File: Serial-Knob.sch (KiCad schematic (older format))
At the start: 17 parts, among them IC1 ATTINY85-S, P1 CONN_4

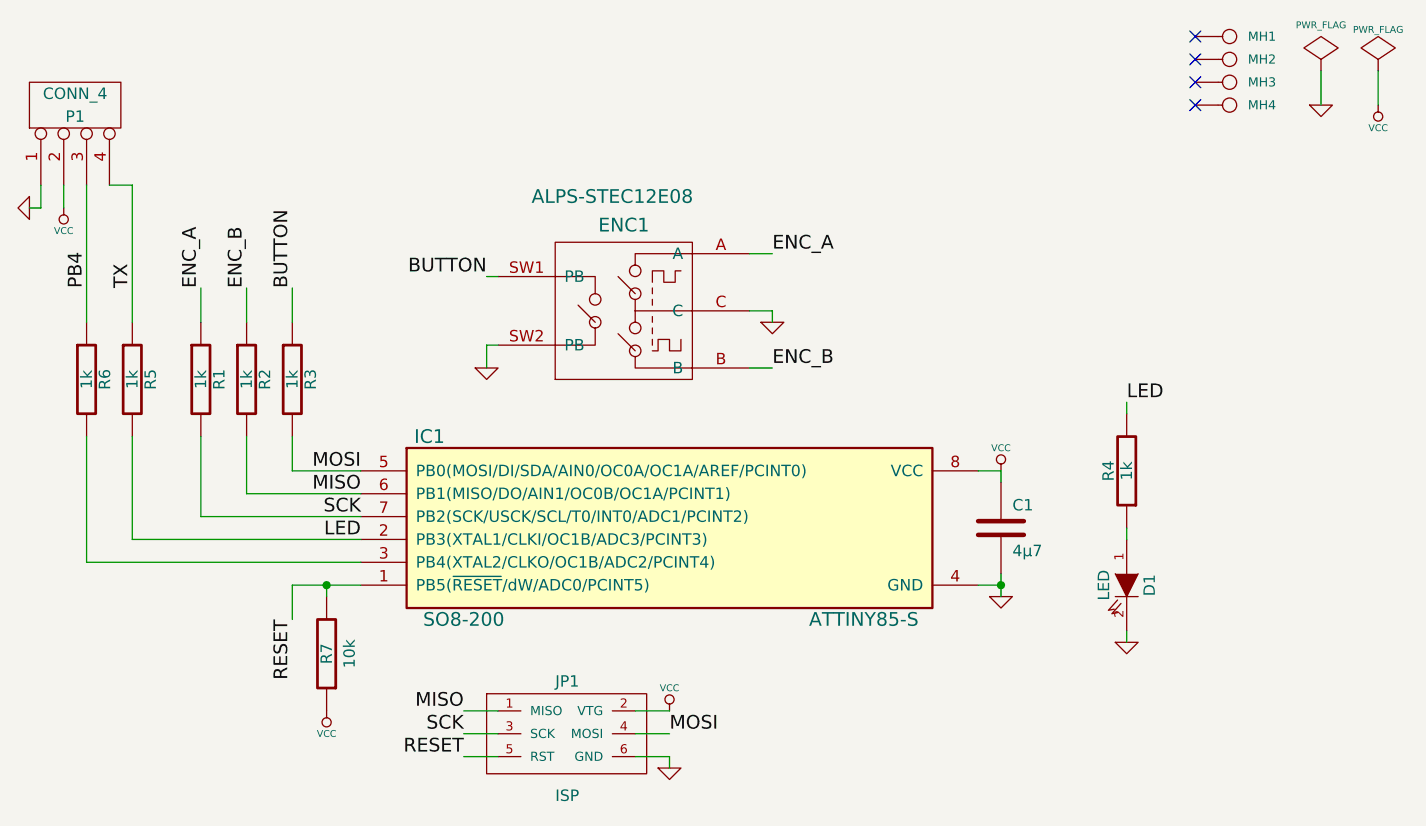
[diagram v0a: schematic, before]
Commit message: Changed all vias to 0.65/0.35 + moved to 1206 resistor packs (4x).
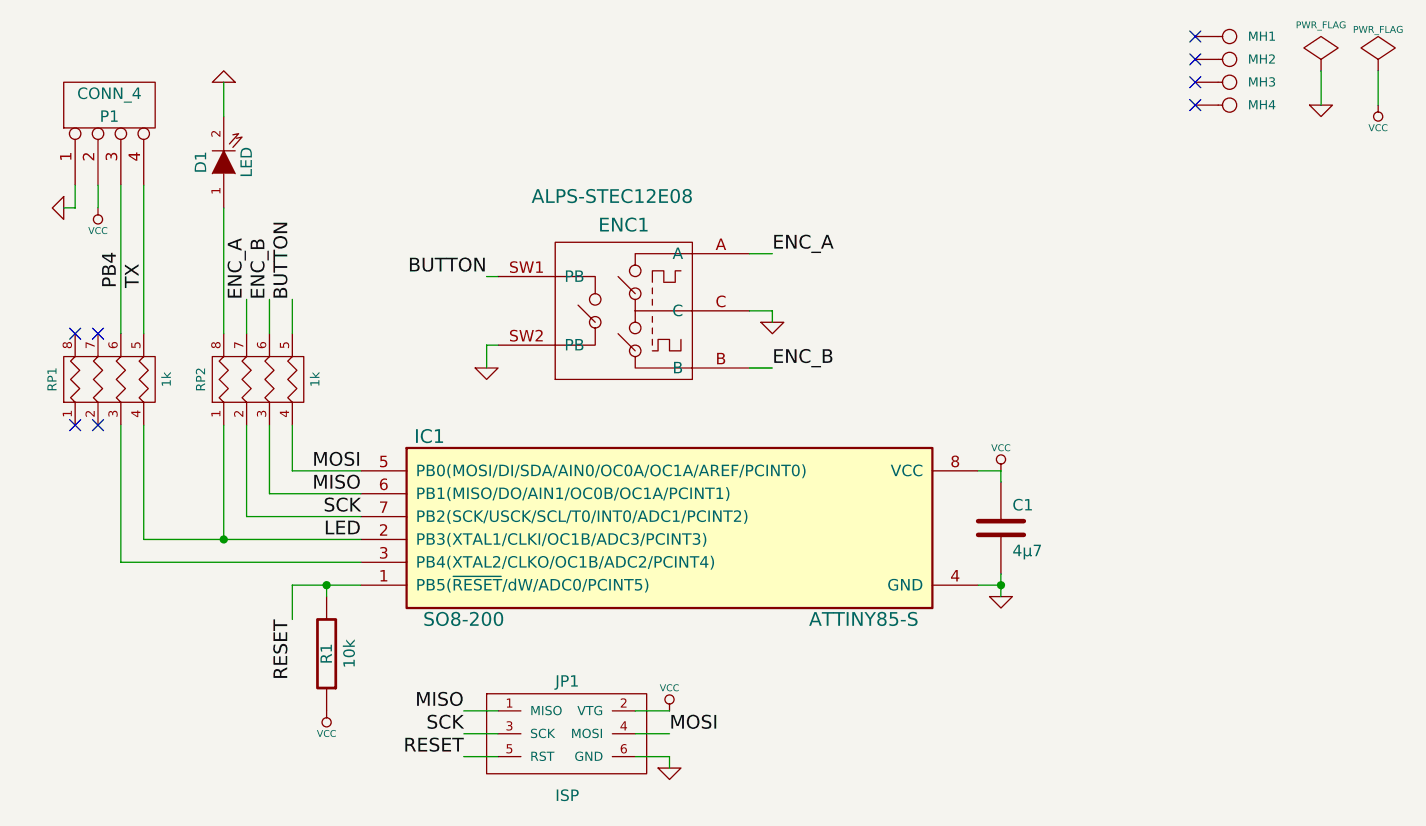
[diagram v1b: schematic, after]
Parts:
- removed R1, R2, R3, R4, R5, R6: 1k, symbol R
- added RP1, RP2: 1k, symbol R_PACK4
- renumbered R7 to R1
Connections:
- net BUTTON: now also RP2.5 (R4)
- net ENC_A: now also RP2.7 (R2)
- net ENC_B: now also RP2.6 (R3)
- net LED: now also RP1.4 (P4), RP2.1 (P1)
- net MISO: now also RP2.3 (P3)
- net MOSI: now also RP2.4 (P4)
- net PB4: now also RP1.6 (R3)
- net SCK: now also RP2.2 (P2)
- net TX: now also RP1.5 (R4)
- net at D1.1 (A): now also RP2.8 (R1)
- net at IC1.3 (PB4(XTAL2/CLKO/OC1B/ADC2/PCINT4)): now also RP1.3 (P3)
- no-connect marks 4 -> 8
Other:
- moved on the sheet: D1, P1
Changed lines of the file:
@@
-EESchema Schematic File Version 2  date Wed 27 Feb 2013 09:12:17 AM CET
+EESchema Schematic File Version 2  date Fri 01 Mar 2013 09:15:15 AM CET
 LIBS:my_parts
 LIBS:power
@@
 Sheet 1 1
 Title "Serial Knob - a.k.a. \"The Knob\""
-Date "23 feb 2013"
-Rev "0.1"
+Date "1 mar 2013"
+Rev "0.2"
 Comp "2013 - blog.spitzenpfeil.org"
 Comment1 ""
@@
 	1    0    0    -1
 $EndComp
-Text Label 2200 1950 1    60   ~ 0
+Text Label 2400 2000 1    60   ~ 0
 ENC_A
-Text Label 2400 1950 1    60   ~ 0
+Text Label 2500 2000 1    60   ~ 0
 ENC_B
-Text Label 2600 1950 1    60   ~ 0
+Text Label 2600 2000 1    60   ~ 0
 BUTTON
 $Comp
@@
 $EndComp
 $Comp
-L R R7
+L R R1
 U 1 1 4F6EC6DD
 P 2750 3550
-F 0 "R7" V 2750 3550 50  0000 C CNN
+F 0 "R1" V 2750 3550 50  0000 C CNN
 F 1 "10k" V 2650 3550 50  0000 C CNN
 F 2 "" H 2750 3550 60  0001 C CNN
@@
 $EndComp
 Connection ~ 2750 3250
-Wire Wire Line
-	2400 2850 2900 2850
-Wire Wire Line
-	2200 2950 2900 2950
 Wire Wire Line
 	2600 3250 2900 3250
@@
 L LED D1
 U 1 1 50EDA6CA
-P 6250 3250
-F 0 "D1" H 6250 3350 50  0000 C CNN
-F 1 "LED" H 6250 3150 50  0000 C CNN
-F 2 "" H 6250 3250 60  0001 C CNN
-F 3 "" H 6250 3250 60  0001 C CNN
-	1    6250 3250
-	0    1    1    0
+P 2300 1400
+F 0 "D1" H 2300 1500 50  0000 C CNN
+F 1 "LED" H 2300 1300 50  0000 C CNN
+F 2 "" H 2300 1400 60  0001 C CNN
+F 3 "" H 2300 1400 60  0001 C CNN
+	1    2300 1400
+	0    -1   -1   0
 $EndComp
 $Comp
 L GND #PWR06
-U 1 1 50EDA6D9
-P 6250 3500
-F 0 "#PWR06" H 6250 3500 30  0001 C CNN
-F 1 "GND" H 6250 3430 30  0001 C CNN
-F 2 "" H 6250 3500 60  0001 C CNN
-F 3 "" H 6250 3500 60  0001 C CNN
-	1    6250 3500
-	1    0    0    -1
-$EndComp
-$Comp
-L R R4
-U 1 1 50EDA6E8
-P 6250 2750
-F 0 "R4" V 6330 2750 50  0000 C CNN
-F 1 "1k" V 6250 2750 50  0000 C CNN
-F 2 "" H 6250 2750 60  0001 C CNN
-F 3 "" H 6250 2750 60  0001 C CNN
-	1    6250 2750
-	-1   0    0    1
-$EndComp
-Wire Wire Line
-	6250 3450 6250 3500
-Wire Wire Line
-	6250 3050 6250 3000
-Wire Wire Line
-	6250 2450 6250 2500
-$Comp
-L GND #PWR07
 U 1 1 50FE45EC
 P 3450 2300
-F 0 "#PWR07" H 3450 2300 30  0001 C CNN
+F 0 "#PWR06" H 3450 2300 30  0001 C CNN
 F 1 "GND" H 3450 2230 30  0001 C CNN
 F 2 "" H 3450 2300 60  0001 C CNN
@@
 	4700 2050 4700 2100
 $Comp
-L GND #PWR08
+L GND #PWR07
 U 1 1 50FE464A
 P 4700 2100
-F 0 "#PWR08" H 4700 2100 30  0001 C CNN
+F 0 "#PWR07" H 4700 2100 30  0001 C CNN
 F 1 "GND" H 4700 2030 30  0001 C CNN
 F 2 "" H 4700 2100 60  0001 C CNN
@@
 Text Label 3450 1900 2    60   ~ 0
 BUTTON
-$Comp
-L R R1
-U 1 1 50FE472E
-P 2200 2350
-F 0 "R1" V 2280 2350 50  0000 C CNN
-F 1 "1k" V 2200 2350 50  0000 C CNN
-F 2 "" H 2200 2350 60  0001 C CNN
-F 3 "" H 2200 2350 60  0001 C CNN
-	1    2200 2350
-	1    0    0    -1
-$EndComp
-$Comp
-L R R2
-U 1 1 50FE473D
-P 2400 2350
-F 0 "R2" V 2480 2350 50  0000 C CNN
-F 1 "1k" V 2400 2350 50  0000 C CNN
-F 2 "" H 2400 2350 60  0001 C CNN
-F 3 "" H 2400 2350 60  0001 C CNN
-	1    2400 2350
-	1    0    0    -1
-$EndComp
-$Comp
-L R R3
-U 1 1 50FE474C
-P 2600 2350
-F 0 "R3" V 2680 2350 50  0000 C CNN
-F 1 "1k" V 2600 2350 50  0000 C CNN
-F 2 "" H 2600 2350 60  0001 C CNN
-F 3 "" H 2600 2350 60  0001 C CNN
-	1    2600 2350
-	1    0    0    -1
-$EndComp
-Wire Wire Line
-	2600 2600 2600 2750
-Wire Wire Line
-	2400 2600 2400 2850
-Wire Wire Line
-	2200 2600 2200 2950
-Wire Wire Line
-	2600 1950 2600 2100
-Wire Wire Line
-	2400 1950 2400 2100
-Wire Wire Line
-	2200 1950 2200 2100
 Wire Wire Line
 	2600 2750 2900 2750
-Text Label 1900 1950 1    60   ~ 0
+Text Label 1950 1950 1    60   ~ 0
 TX
 Wire Wire Line
@@
 Text Label 2900 3050 2    60   ~ 0
 LED
-Text Label 6250 2450 0    60   ~ 0
-LED
 $Comp
 L CONN_4 P1
 U 1 1 50FE4A96
-P 1650 1150
-F 0 "P1" V 1600 1150 50  0000 C CNN
-F 1 "CONN_4" V 1700 1150 50  0000 C CNN
-F 2 "" H 1650 1150 60  0001 C CNN
-F 3 "" H 1650 1150 60  0001 C CNN
-	1    1650 1150
+P 1800 1150
+F 0 "P1" V 1750 1150 50  0000 C CNN
+F 1 "CONN_4" V 1850 1150 50  0000 C CNN
+F 2 "" H 1800 1150 60  0001 C CNN
+F 3 "" H 1800 1150 60  0001 C CNN
+	1    1800 1150
 	0    -1   -1   0
 $EndComp
 Wire Wire Line
-	1600 1500 1600 1600
-Wire Wire Line
-	1500 1500 1500 1600
-$Comp
-L GND #PWR09
+	1750 1500 1750 1600
+Wire Wire Line
+	1650 1500 1650 1600
+$Comp
+L GND #PWR08
 U 1 1 50FE4B02
-P 1450 1600
-F 0 "#PWR09" H 1450 1600 30  0001 C CNN
-F 1 "GND" H 1450 1530 30  0001 C CNN
-F 2 "" H 1450 1600 60  0001 C CNN
-F 3 "" H 1450 1600 60  0001 C CNN
-	1    1450 1600
-	0    1    1    0
-$EndComp
-Wire Wire Line
-	1500 1600 1450 1600
-$Comp
-L VCC #PWR010
-U 1 1 50FE4B43
 P 1600 1600
-F 0 "#PWR010" H 1600 1700 30  0001 C CNN
-F 1 "VCC" H 1600 1700 30  0000 C CNN
+F 0 "#PWR08" H 1600 1600 30  0001 C CNN
+F 1 "GND" H 1600 1530 30  0001 C CNN
 F 2 "" H 1600 1600 60  0001 C CNN
 F 3 "" H 1600 1600 60  0001 C CNN
 	1    1600 1600
+	0    1    1    0
+$EndComp
+Wire Wire Line
+	1650 1600 1600 1600
+$Comp
+L VCC #PWR09
+U 1 1 50FE4B43
+P 1750 1600
+F 0 "#PWR09" H 1750 1700 30  0001 C CNN
+F 1 "VCC" H 1750 1700 30  0000 C CNN
+F 2 "" H 1750 1600 60  0001 C CNN
+F 3 "" H 1750 1600 60  0001 C CNN
+	1    1750 1600
 	-1   0    0    1
 $EndComp
@@
 NoConn ~ 6550 950
 NoConn ~ 6550 850
-$Comp
-L R R5
-U 1 1 50FE56B2
-P 1900 2350
-F 0 "R5" V 1980 2350 50  0000 C CNN
-F 1 "1k" V 1900 2350 50  0000 C CNN
-F 2 "" H 1900 2350 60  0001 C CNN
-F 3 "" H 1900 2350 60  0001 C CNN
-	1    1900 2350
-	1    0    0    -1
-$EndComp
-$Comp
-L R R6
-U 1 1 50FE56C1
-P 1700 2350
-F 0 "R6" V 1780 2350 50  0000 C CNN
-F 1 "1k" V 1700 2350 50  0000 C CNN
-F 2 "" H 1700 2350 60  0001 C CNN
-F 3 "" H 1700 2350 60  0001 C CNN
-	1    1700 2350
-	1    0    0    -1
-$EndComp
-Wire Wire Line
-	1700 1500 1700 2100
-Text Label 1700 1950 1    60   ~ 0
+Text Label 1850 1950 1    60   ~ 0
 PB4
 $Comp
-L PWR_FLAG #FLG011
+L PWR_FLAG #FLG010
 U 1 1 50FE5769
 P 7350 1000
-F 0 "#FLG011" H 7350 1095 30  0001 C CNN
+F 0 "#FLG010" H 7350 1095 30  0001 C CNN
 F 1 "PWR_FLAG" H 7350 1180 30  0000 C CNN
 F 2 "" H 7350 1000 60  0001 C CNN
@@
 $EndComp
 $Comp
-L VCC #PWR012
+L VCC #PWR011
 U 1 1 50FE5778
 P 7350 1150
-F 0 "#PWR012" H 7350 1250 30  0001 C CNN
+F 0 "#PWR011" H 7350 1250 30  0001 C CNN
 F 1 "VCC" H 7350 1250 30  0000 C CNN
 F 2 "" H 7350 1150 60  0001 C CNN
@@
 Wire Wire Line
 	7350 1000 7350 1150
-Wire Wire Line
-	1900 1500 1900 2100
-Wire Wire Line
-	1900 2600 1900 3050
-Wire Wire Line
-	1900 3050 2900 3050
-Wire Wire Line
-	1700 2600 1700 3150
-Wire Wire Line
-	1700 3150 2900 3150
-Wire Wire Line
-	1800 1500 1900 1500
 Text Label 4250 3900 0    60   ~ 0
 MOSI
@@
 $EndComp
 $Comp
-L VCC #PWR013
+L VCC #PWR012
 U 1 1 50FF0F17
 P 4250 3800
-F 0 "#PWR013" H 4250 3900 30  0001 C CNN
+F 0 "#PWR012" H 4250 3900 30  0001 C CNN
 F 1 "VCC" H 4250 3900 30  0000 C CNN
 F 2 "" H 4250 3800 60  0001 C CNN
@@
 $EndComp
 $Comp
-L GND #PWR014
+L GND #PWR013
 U 1 1 50FF0F26
 P 4250 4050
-F 0 "#PWR014" H 4250 4050 30  0001 C CNN
+F 0 "#PWR013" H 4250 4050 30  0001 C CNN
 F 1 "GND" H 4250 3980 30  0001 C CNN
 F 2 "" H 4250 4050 60  0001 C CNN
@@
 	1    0    0    -1
 $EndComp
+$Comp
+L R_PACK4 RP2
+U 1 1 51305629
+P 2650 2350
+F 0 "RP2" H 2650 2800 40  0000 C CNN
+F 1 "1k" H 2650 2300 40  0000 C CNN
+F 2 "" H 2650 2350 60  0000 C CNN
+F 3 "" H 2650 2350 60  0000 C CNN
+	1    2650 2350
+	0    -1   -1   0
+$EndComp
+$Comp
+L R_PACK4 RP1
+U 1 1 51305642
+P 2000 2350
+F 0 "RP1" H 2000 2800 40  0000 C CNN
+F 1 "1k" H 2000 2300 40  0000 C CNN
+F 2 "" H 2000 2350 60  0000 C CNN
+F 3 "" H 2000 2350 60  0000 C CNN
+	1    2000 2350
+	0    -1   -1   0
+$EndComp
+Wire Wire Line
+	2600 2550 2600 2750
+Wire Wire Line
+	2500 2550 2500 2850
+Wire Wire Line
+	2400 2550 2400 2950
+Wire Wire Line
+	2500 2850 2900 2850
+Wire Wire Line
+	2400 2950 2900 2950
+Wire Wire Line
+	2300 2550 2300 3050
+Wire Wire Line
+	1950 3050 2900 3050
+Wire Wire Line
+	1950 3050 1950 2550
+Connection ~ 2300 3050
+Wire Wire Line
+	2600 2000 2600 2150
+Wire Wire Line
+	2500 2000 2500 2150
+Wire Wire Line
+	2400 2000 2400 2150
+Wire Wire Line
+	2300 1600 2300 2150
+$Comp
+L GND #PWR014
+U 1 1 51305895
+P 2300 1050
+F 0 "#PWR014" H 2300 1050 30  0001 C CNN
+F 1 "GND" H 2300 980 30  0001 C CNN
+F 2 "" H 2300 1050 60  0000 C CNN
+F 3 "" H 2300 1050 60  0000 C CNN
+	1    2300 1050
+	-1   0    0    1
+$EndComp
+Wire Wire Line
+	2300 1050 2300 1200
+Wire Wire Line
+	1950 1500 1950 2150
+Wire Wire Line
+	1850 1500 1850 2150
+Wire Wire Line
+	1850 2550 1850 3150
+Wire Wire Line
+	1850 3150 2900 3150
+NoConn ~ 1650 2550
+NoConn ~ 1750 2550
+NoConn ~ 1750 2150
+NoConn ~ 1650 2150
 $EndSCHEMATC

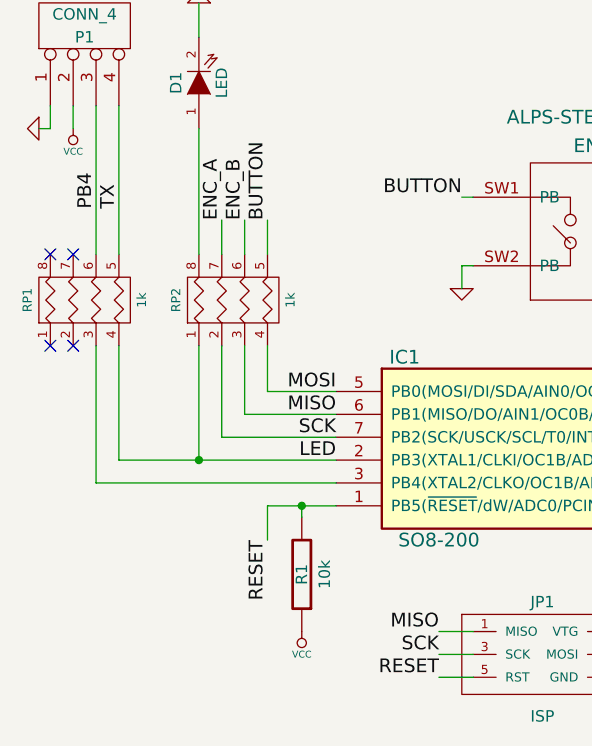
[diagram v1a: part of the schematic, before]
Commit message: Eliminated reset pullup by using unused rpack pins + now one 2.2k rpack.
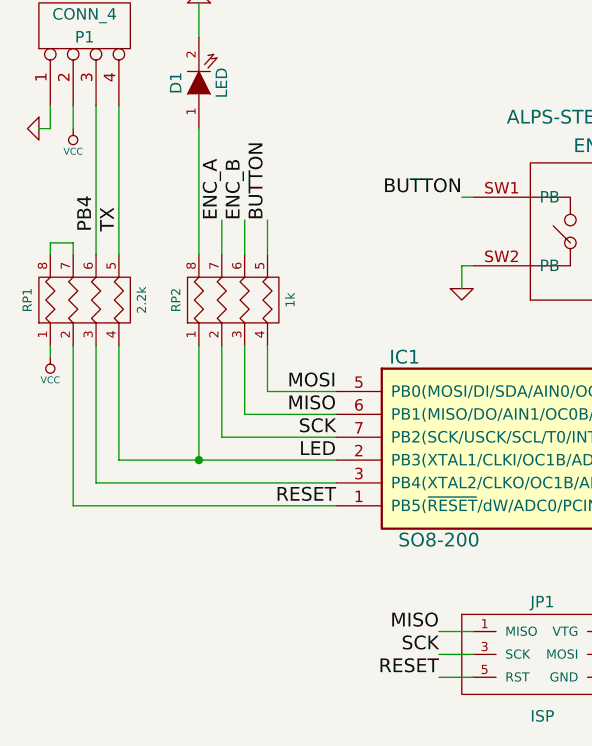
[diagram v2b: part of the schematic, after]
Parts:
- removed R1: 10k, symbol R
- RP1: value 1k -> 2.2k
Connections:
- net RESET: now also RP1.2 (P2)
- net VCC: now also RP1.1 (P1)
- net at RP1.7 (R2): now also RP1.8 (R1)
- no-connect marks 8 -> 4
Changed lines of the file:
@@
-EESchema Schematic File Version 2  date Fri 01 Mar 2013 09:15:15 AM CET
+EESchema Schematic File Version 2  date Fri 01 Mar 2013 01:11:33 PM CET
 LIBS:my_parts
 LIBS:power
@@
 	5700 2750 5600 2750
 Wire Wire Line
-	2750 3250 2750 3300
-Wire Wire Line
 	5700 3250 5600 3250
 Wire Wire Line
@@
 	1    0    0    -1
 $EndComp
-Text Label 2600 3400 3    60   ~ 0
+Text Label 2900 3250 2    60   ~ 0
 RESET
 $Comp
@@
 L VCC #PWR03
 U 1 1 4F6EE70F
-P 2750 3800
-F 0 "#PWR03" H 2750 3900 30  0001 C CNN
-F 1 "VCC" H 2750 3900 30  0000 C CNN
-F 2 "" H 2750 3800 60  0001 C CNN
-F 3 "" H 2750 3800 60  0001 C CNN
-	1    2750 3800
+P 1650 2600
+F 0 "#PWR03" H 1650 2700 30  0001 C CNN
+F 1 "VCC" H 1650 2700 30  0000 C CNN
+F 2 "" H 1650 2600 60  0001 C CNN
+F 3 "" H 1650 2600 60  0001 C CNN
+	1    1650 2600
 	-1   0    0    1
 $EndComp
-$Comp
-L R R1
-U 1 1 4F6EC6DD
-P 2750 3550
-F 0 "R1" V 2750 3550 50  0000 C CNN
-F 1 "10k" V 2650 3550 50  0000 C CNN
-F 2 "" H 2750 3550 60  0001 C CNN
-F 3 "" H 2750 3550 60  0001 C CNN
-	1    2750 3550
-	-1   0    0    1
-$EndComp
-Connection ~ 2750 3250
-Wire Wire Line
-	2600 3250 2900 3250
+Wire Wire Line
+	1750 3250 2900 3250
 $Comp
 L PWR_FLAG #FLG04
@@
 Wire Wire Line
 	2600 2750 2900 2750
-Text Label 1950 1950 1    60   ~ 0
+Text Label 1950 2050 1    60   ~ 0
 TX
-Wire Wire Line
-	2600 3250 2600 3400
 Text Label 2900 3050 2    60   ~ 0
 LED
@@
 NoConn ~ 6550 950
 NoConn ~ 6550 850
-Text Label 1850 1950 1    60   ~ 0
+Text Label 1850 2050 1    60   ~ 0
 PB4
 $Comp
@@
 	0    -1   -1   0
 $EndComp
-$Comp
-L R_PACK4 RP1
-U 1 1 51305642
-P 2000 2350
-F 0 "RP1" H 2000 2800 40  0000 C CNN
-F 1 "1k" H 2000 2300 40  0000 C CNN
-F 2 "" H 2000 2350 60  0000 C CNN
-F 3 "" H 2000 2350 60  0000 C CNN
-	1    2000 2350
-	0    -1   -1   0
-$EndComp
 Wire Wire Line
 	2600 2550 2600 2750
@@
 Wire Wire Line
 	1850 3150 2900 3150
-NoConn ~ 1650 2550
-NoConn ~ 1750 2550
-NoConn ~ 1750 2150
-NoConn ~ 1650 2150
+$Comp
+L R_PACK4 RP1
+U 1 1 51305642
+P 2000 2350
+F 0 "RP1" H 2000 2800 40  0000 C CNN
+F 1 "2.2k" H 2000 2300 40  0000 C CNN
+F 2 "" H 2000 2350 60  0000 C CNN
+F 3 "" H 2000 2350 60  0000 C CNN
+	1    2000 2350
+	0    -1   -1   0
+$EndComp
+Wire Wire Line
+	1750 3250 1750 2550
+Wire Wire Line
+	1650 2550 1650 2600
+Wire Wire Line
+	1750 2150 1750 2100
+Wire Wire Line
+	1750 2100 1650 2100
+Wire Wire Line
+	1650 2100 1650 2150
 $EndSCHEMATC

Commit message: ENC footprint made to fit EN11-HSM1AF15. Need to do it properly later.
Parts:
- ENC1: value ALPS-STEC12E08 -> EN11-HSM1AF15
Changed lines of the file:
@@
-EESchema Schematic File Version 2  date Fri 01 Mar 2013 01:11:33 PM CET
+EESchema Schematic File Version 2  date Sat 02 Mar 2013 05:01:35 AM CET
 LIBS:my_parts
 LIBS:power
@@
 Sheet 1 1
 Title "Serial Knob - a.k.a. \"The Knob\""
-Date "1 mar 2013"
+Date "2 mar 2013"
 Rev "0.2"
 Comp "2013 - blog.spitzenpfeil.org"
@@
 P 4050 2050
 F 0 "ENC1" H 4050 2425 60  0000 C CNN
-F 1 "ALPS-STEC12E08" H 4000 2550 60  0000 C CNN
+F 1 "EN11-HSM1AF15" H 4000 2550 60  0000 C CNN
 F 2 "" H 4050 2050 60  0000 C CNN
 F 3 "" H 4050 2050 60  0000 C CNN
